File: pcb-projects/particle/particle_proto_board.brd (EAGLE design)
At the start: 33.7 x 30.5 mm, 35 parts, among them IC1 ATTINY20-MMH, IC2 DMC2400V, IC3 DMC2400V, SW1 T/S-PI SW, SW2 T/S-PI SW, SW3 T/S-PI SW

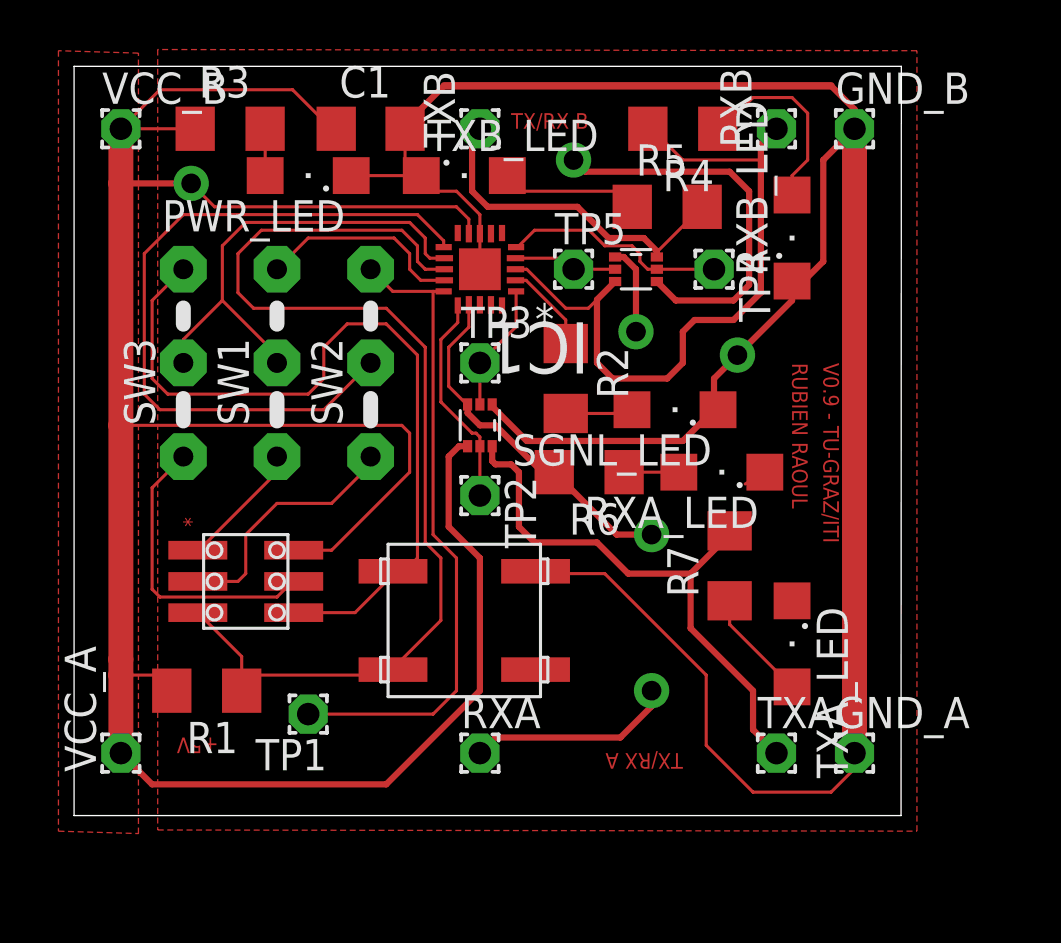
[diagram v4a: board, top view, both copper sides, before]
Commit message: changed all resistors 1k -> 150
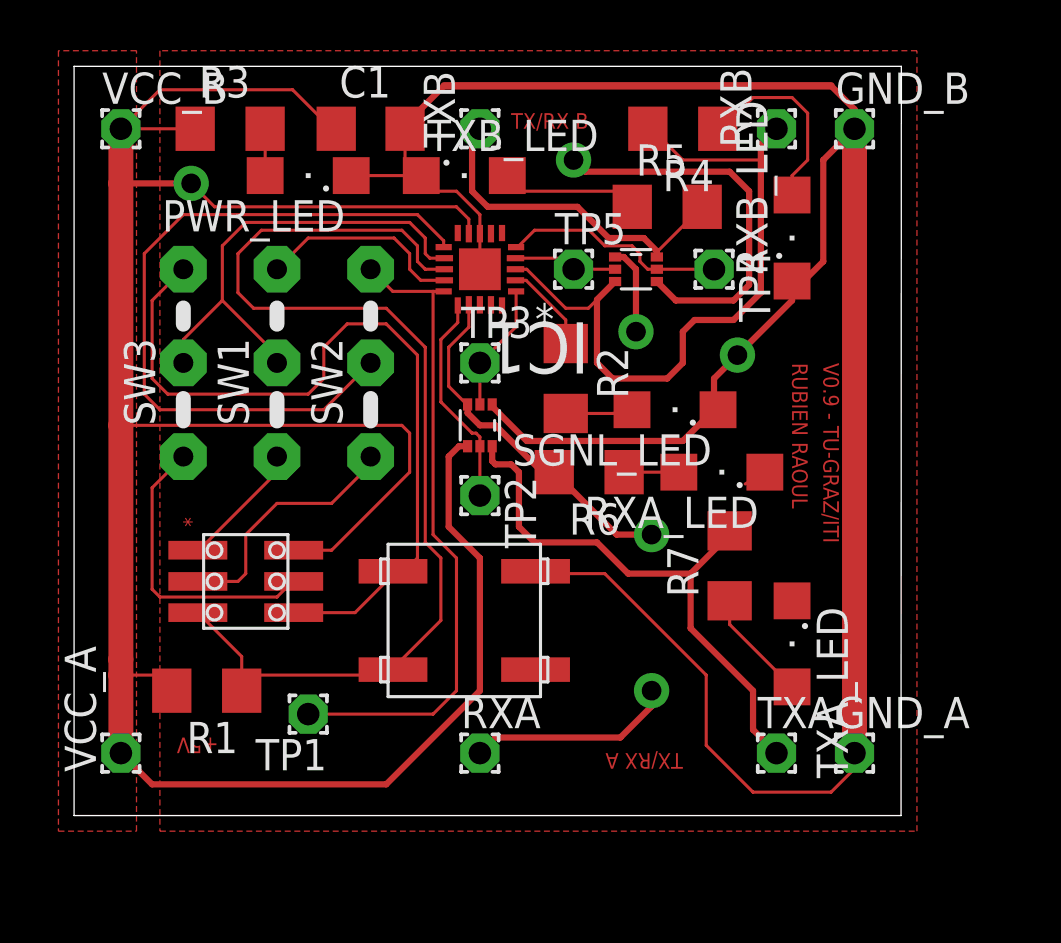
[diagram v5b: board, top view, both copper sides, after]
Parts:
- R1, R2, R3, R4, R5, R6, R7: value 1k -> 150
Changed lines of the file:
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@@
 <?xml version="1.0" encoding="utf-8"?>
 <!DOCTYPE eagle SYSTEM "eagle.dtd">
-<eagle version="6.5.0">
+<eagle version="7.2.0">
 <drawing>
 <settings>
@@
 <setting verticaltext="up"/>
 </settings>
-<grid distance="0.003125" unitdist="mic" unit="mm" style="lines" multiple="1" display="yes" altdistance="0.00625" altunitdist="inch" altunit="inch"/>
+<grid distance="12.5" unitdist="mil" unit="mil" style="lines" multiple="1" display="yes" altdistance="0.00625" altunitdist="inch" altunit="inch"/>
 <layers>
 <layer number="1" name="Top" color="4" fill="1" visible="yes" active="yes"/>
@@
 <pass name="Default">
 <param name="RoutingGrid" value="6.25mil"/>
+<param name="AutoGrid" value="1"/>
+<param name="Efforts" value="0"/>
+<param name="TopRouterVariant" value="1"/>
 <param name="tpViaShape" value="round"/>
 <param name="PrefDir.1" value="*"/>
@@
 <elements>
 <element name="IC1" library="tiny_particles_MCU" package="QFN45P300X300X85-21N" value="ATTINY20-MMH" x="16.51" y="22.225" rot="R180"/>
-<element name="R2" library="rcl" package="R1206" value="1k" x="20.0025" y="17.78" rot="R270"/>
+<element name="R2" library="rcl" package="R1206" value="150" x="20.0025" y="17.78" rot="R270"/>
 <element name="SGNL_LED" library="led" package="SML1206" value="GRN" x="24.4475" y="16.51" rot="R180"/>
 <element name="IC3" library="diodes" package="SOT563" value="DMC2400V" x="22.86" y="22.225" rot="R270"/>
-<element name="R5" library="rcl" package="R1206" value="1k" x="24.13" y="24.765"/>
+<element name="R5" library="rcl" package="R1206" value="150" x="24.13" y="24.765"/>
 <element name="TXB_LED" library="led" package="SML1206" value="RED" x="15.875" y="26.035"/>
 <element name="RXB_LED" library="led" package="SML1206" value="GRN" x="29.21" y="23.495" rot="R90"/>
-<element name="R4" library="rcl" package="R1206" value="1k" x="24.765" y="27.94" rot="R180"/>
+<element name="R4" library="rcl" package="R1206" value="150" x="24.765" y="27.94" rot="R180"/>
 <element name="IC2" library="diodes" package="SOT563" value="DMC2400V" x="16.51" y="15.875" rot="R180"/>
-<element name="R7" library="rcl" package="R1206" value="1k" x="26.67" y="10.16" rot="R90"/>
+<element name="R7" library="rcl" package="R1206" value="150" x="26.67" y="10.16" rot="R90"/>
 <element name="TXA_LED" library="led" package="SML1206" value="RED" x="29.21" y="6.985" rot="R270"/>
 <element name="RXA_LED" library="led" package="SML1206" value="GRN" x="26.3525" y="13.97" rot="R180"/>
-<element name="R6" library="rcl" package="R1206" value="1k" x="20.955" y="13.97" rot="R180"/>
-<element name="R1" library="rcl" package="R1206" value="1k" x="5.3975" y="5.08" rot="R180"/>
+<element name="R6" library="rcl" package="R1206" value="150" x="20.955" y="13.97" rot="R180"/>
+<element name="R1" library="rcl" package="R1206" value="150" x="5.3975" y="5.08" rot="R180"/>
 <element name="C1" library="rcl" package="C1206" value="100n" x="12.065" y="27.94"/>
 <element name="TP1" library="wirepad" package="1,6/0,9" value="TP1" x="9.525" y="4.1275" rot="R180"/>
@@
 <element name="RXA" library="wirepad" package="1,6/0,9" value="RXA" x="16.51" y="2.54"/>
 <element name="TXA" library="wirepad" package="1,6/0,9" value="TXA" x="28.575" y="2.54"/>
-<element name="R3" library="rcl" package="R1206" value="1k" x="6.35" y="27.94"/>
+<element name="R3" library="rcl" package="R1206" value="150" x="6.35" y="27.94"/>
 <element name="PWR_LED" library="led" package="SML1206" value="RED" x="9.525" y="26.035" rot="R180"/>
 <element name="SW1" library="jumper-switches" package="04C" value="T/S-PI SW" x="8.255" y="16.51" rot="R90"/>
@@
 <contactref element="PWR_LED" pad="C"/>
 <polygon width="0.127" layer="1" isolate="0.6096">
-<vertex x="3.40245" y="31.163734375"/>
-<vertex x="3.40245" y="-0.586265625"/>
+<vertex x="3.4925" y="31.115"/>
+<vertex x="3.4925" y="-0.635"/>
 <vertex x="34.29" y="-0.635"/>
 <vertex x="34.29" y="31.115"/>
@@
 <contactref element="R3" pad="1"/>
 <polygon width="0.127" layer="1" isolate="0.6096">
-<vertex x="2.619234375" y="31.01753125"/>
+<vertex x="2.54" y="31.115"/>
 <vertex x="-0.635" y="31.115"/>
 <vertex x="-0.635" y="-0.635"/>
-<vertex x="2.619234375" y="-0.73246875"/>
+<vertex x="2.54" y="-0.635"/>
 </polygon>
 <wire x1="23.71" y1="21.725" x2="24.48" y2="20.955" width="0.254" layer="1"/>

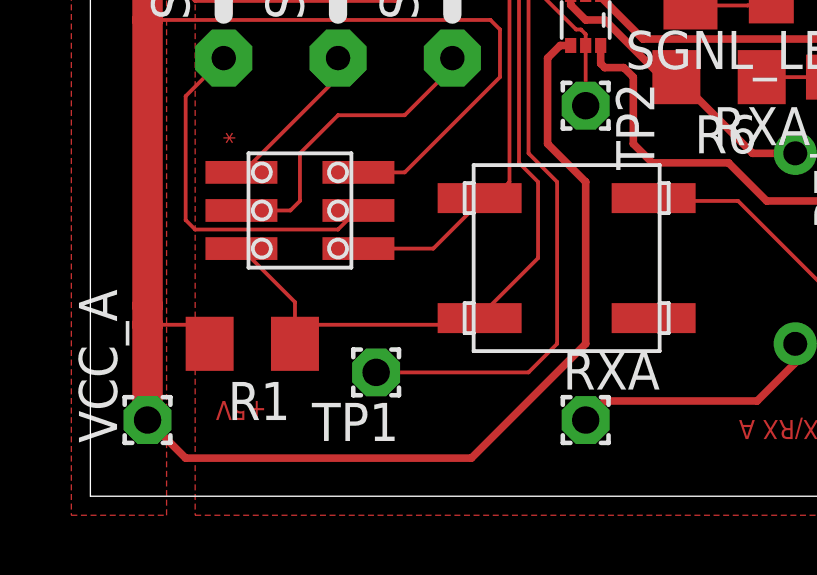
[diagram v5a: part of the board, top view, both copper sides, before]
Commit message: cosmetics: moved 5V label and testpoint 1 smome mm
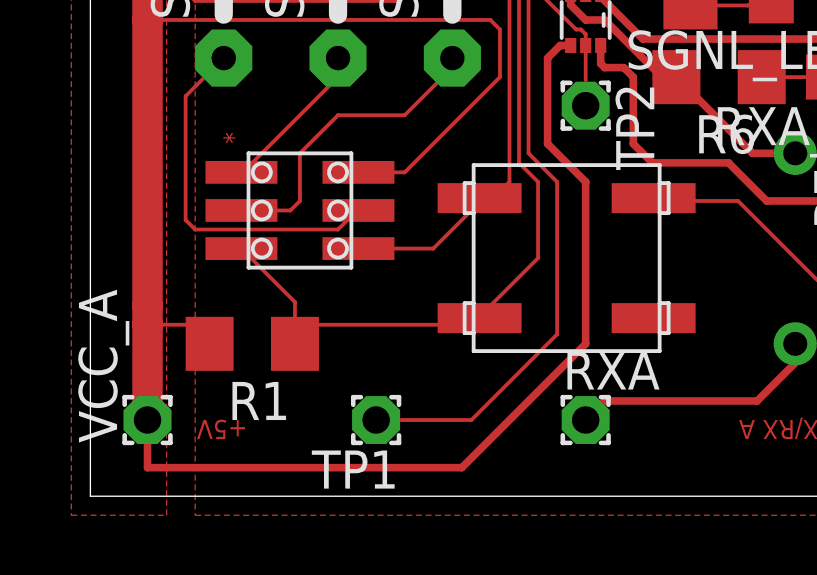
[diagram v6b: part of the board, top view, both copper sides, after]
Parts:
- SGNL_LED: value GRN -> ORNG
- moved TP1 1.59 mm to (9.53, 2.54)
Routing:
- net VCC: track 119.5 -> 120.7 mm
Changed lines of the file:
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@@
 <layer number="19" name="Unrouted" color="6" fill="1" visible="yes" active="yes"/>
 <layer number="20" name="Dimension" color="15" fill="1" visible="yes" active="yes"/>
-<layer number="21" name="tPlace" color="7" fill="1" visible="yes" active="yes"/>
+<layer number="21" name="tPlace" color="7" fill="1" visible="no" active="yes"/>
 <layer number="22" name="bPlace" color="7" fill="1" visible="no" active="yes"/>
 <layer number="23" name="tOrigins" color="15" fill="1" visible="yes" active="yes"/>
@@
 <wire x1="0" y1="30.48" x2="0" y2="0" width="0" layer="20"/>
 <text x="29.21" y="18.415" size="0.635" layer="1" font="vector" ratio="23" distance="8" rot="SR270">RUBIEN RAOUL</text>
-<text x="5.87375" y="3.175" size="0.635" layer="1" font="vector" ratio="20" distance="8" rot="SR180">+5V</text>
+<text x="5.23875" y="2.54" size="0.635" layer="1" font="vector" ratio="20" distance="8" rot="SR180">+5V</text>
 <text x="17.78" y="27.94" size="0.635" layer="1" font="vector" ratio="20" distance="8" rot="SR0">TX/RX B</text>
 <text x="24.765" y="2.54" size="0.635" layer="1" font="vector" ratio="20" distance="8" rot="SR180">TX/RX A</text>
@@
 <text x="29.21" y="18.415" size="0.635" layer="29" font="vector" ratio="23" distance="8" rot="SR270">RUBIEN RAOUL</text>
 <text x="24.765" y="2.54" size="0.635" layer="29" font="vector" ratio="20" distance="8" rot="SR180">TX/RX A</text>
-<text x="5.87375" y="3.175" size="0.635" layer="29" font="vector" ratio="20" distance="0" rot="SR180">+5V</text>
+<text x="5.23875" y="2.54" size="0.635" layer="29" font="vector" ratio="20" distance="0" rot="SR180">+5V</text>
 <text x="17.78" y="27.94" size="0.635" layer="29" font="vector" ratio="20" distance="8" rot="SR0">TX/RX B</text>
 <wire x1="1.27" y1="27.94" x2="1.27" y2="2.54" width="1.016" layer="29"/>
@@
 <element name="IC1" library="tiny_particles_MCU" package="QFN45P300X300X85-21N" value="ATTINY20-MMH" x="16.51" y="22.225" rot="R180"/>
 <element name="R2" library="rcl" package="R1206" value="150" x="20.0025" y="17.78" rot="R270"/>
-<element name="SGNL_LED" library="led" package="SML1206" value="GRN" x="24.4475" y="16.51" rot="R180"/>
+<element name="SGNL_LED" library="led" package="SML1206" value="ORNG" x="24.4475" y="16.51" rot="R180"/>
 <element name="IC3" library="diodes" package="SOT563" value="DMC2400V" x="22.86" y="22.225" rot="R270"/>
 <element name="R5" library="rcl" package="R1206" value="150" x="24.13" y="24.765"/>
@@
 <element name="R1" library="rcl" package="R1206" value="150" x="5.3975" y="5.08" rot="R180"/>
 <element name="C1" library="rcl" package="C1206" value="100n" x="12.065" y="27.94"/>
-<element name="TP1" library="wirepad" package="1,6/0,9" value="TP1" x="9.525" y="4.1275" rot="R180"/>
+<element name="TP1" library="wirepad" package="1,6/0,9" value="TP1" x="9.525" y="2.54" rot="R180"/>
 <element name="TP3" library="wirepad" package="1,6/0,9" value="TP3" x="16.51" y="18.415"/>
 <element name="TP2" library="wirepad" package="1,6/0,9" value="TP2" x="16.51" y="13.0175" rot="R270"/>
@@
 <wire x1="13.0175" y1="9.8425" x2="11.43" y2="8.255" width="0.127" layer="1"/>
 <wire x1="13.335" y1="9.8425" x2="13.97" y2="10.4775" width="0.127" layer="1"/>
-<wire x1="26.035" y1="17.78" x2="22.86" y2="19.685" width="0" layer="19" extent="1-1"/>
-<wire x1="13.97" y1="18.7325" x2="17.01" y2="16.725" width="0" layer="19" extent="1-1"/>
+<wire x1="17.01" y1="16.725" x2="13.97" y2="18.7325" width="0" layer="19" extent="1-1"/>
+<wire x1="22.86" y1="19.685" x2="26.035" y2="17.78" width="0" layer="19" extent="1-1"/>
 </signal>
 <signal name="PWR/TX_B">
@@
 <wire x1="14.605" y1="21.325" x2="14.605" y2="11.43" width="0.127" layer="1"/>
 <wire x1="14.605" y1="11.43" x2="15.5575" y2="10.4775" width="0.127" layer="1"/>
-<wire x1="15.5575" y1="10.4775" x2="15.5575" y2="5.08" width="0.127" layer="1"/>
-<wire x1="9.525" y1="4.1275" x2="14.605" y2="4.1275" width="0.127" layer="1"/>
-<wire x1="14.605" y1="4.1275" x2="15.5575" y2="5.08" width="0.127" layer="1"/>
+<wire x1="15.5575" y1="10.4775" x2="15.5575" y2="5.3975" width="0.127" layer="1"/>
+<wire x1="9.525" y1="2.54" x2="12.7" y2="2.54" width="0.127" layer="1"/>
+<wire x1="12.7" y1="2.54" x2="15.5575" y2="5.3975" width="0.127" layer="1"/>
 </signal>
 <signal name="VCC" class="1">
@@
 <wire x1="15.24" y1="11.7475" x2="16.51" y2="10.4775" width="0.254" layer="1"/>
 <wire x1="16.51" y1="10.4775" x2="16.51" y2="5.08" width="0.254" layer="1"/>
-<wire x1="16.51" y1="5.08" x2="12.7" y2="1.27" width="0.254" layer="1"/>
+<wire x1="16.51" y1="5.08" x2="12.3825" y2="0.9525" width="0.254" layer="1"/>
 <wire x1="4.7625" y1="25.7175" x2="1.905" y2="25.7175" width="0.254" layer="1"/>
 <wire x1="15.5575" y1="24.765" x2="5.715" y2="24.765" width="0.127" layer="1"/>
@@
 <wire x1="4.1275" y1="5.715" x2="1.905" y2="5.715" width="0.127" layer="1"/>
 <wire x1="27.46375" y1="25.4" x2="26.67" y2="26.19375" width="0.254" layer="1"/>
-<wire x1="1.905" y1="2.54" x2="3.175" y2="1.27" width="0.254" layer="1"/>
-<wire x1="3.175" y1="1.27" x2="12.7" y2="1.27" width="0.254" layer="1"/>
+<wire x1="1.905" y1="0.9525" x2="12.3825" y2="0.9525" width="0.254" layer="1"/>
+<wire x1="1.905" y1="0.9525" x2="1.905" y2="2.54" width="0.254" layer="1"/>
 <wire x1="16.06" y1="24.2625" x2="20.32" y2="26.67" width="0" layer="19" extent="1-1"/>
 <wire x1="3.9755" y1="5.08" x2="4.1275" y2="5.715" width="0" layer="19" extent="1-1"/>
